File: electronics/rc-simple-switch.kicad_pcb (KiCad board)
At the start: 2 copper layers, 9 parts, among them K1 CONN_3, K2 CONN_3, P1 CONN_5, Q1 PMV30UN, U1 PIC10F200

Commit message: Tweak the PCB
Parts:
- added P2: CONN_1, Test_pad_1mm, F.Cu at (41.0, 41.0)
- added P3: CONN_1, Test_pad_1mm, F.Cu at (46.0, 38.0)
- added P4: CONN_1, Test_pad_1mm, F.Cu at (41.0, 39.5)
- added P5: CONN_1, Test_pad_1mm, F.Cu at (46.0, 39.5)
- P1: value CONN_5 -> CONN_1; footprint debug_connector -> Test_pad_1mm
- moved R2 5.69 mm to (45.0, 42.9), turned to 270 degrees
- moved C1 4.04 mm to (42.7, 42.9), turned to 270 degrees
- moved Q1 2.74 mm to (47.8, 42.4)
- moved U1 2.71 mm to (43.5, 39.5)
- moved K2 2.54 mm to (50.8, 40.6)
- moved P1 2.47 mm to (41.0, 38.0)
- moved R1 0.52 mm to (38.9, 38.9)
- moved D1 0.40 mm to (38.9, 42.4), turned to 0 degrees
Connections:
- P1 pad 1: VSS -> N-000005
- R1 pad 2: /ICSPDAT -> N-000005
- U1 pad 1: /ICSPDAT -> N-000005
- U1 pad 3: /ICSPCLK -> N-000004
- U1 pad 6: /VPP -> N-000003
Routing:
- net VSS: track 36.6 -> 18.4 mm, vias 3 -> 0
- net /ICSPCLK: track 6.70 -> 0.00 mm
- net /ICSPDAT: track 5.95 -> 0.00 mm
- net /OUT: track 10.6 -> 4.69 mm
- net VDD: track 13.1 -> 7.88 mm
- net VCC: track 23.7 -> 19.2 mm
- net N-000005: track 0.00 -> 4.35 mm
- net /VPP: track 2.59 -> 0.00 mm
- net N-000004: track 0.00 -> 1.46 mm
- net N-000003: track 0.00 -> 1.46 mm
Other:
- net class Power added: clearance 0.508, trace_width 0.254, via_dia 0.889, via_drill 0.635
- board text added: "1"

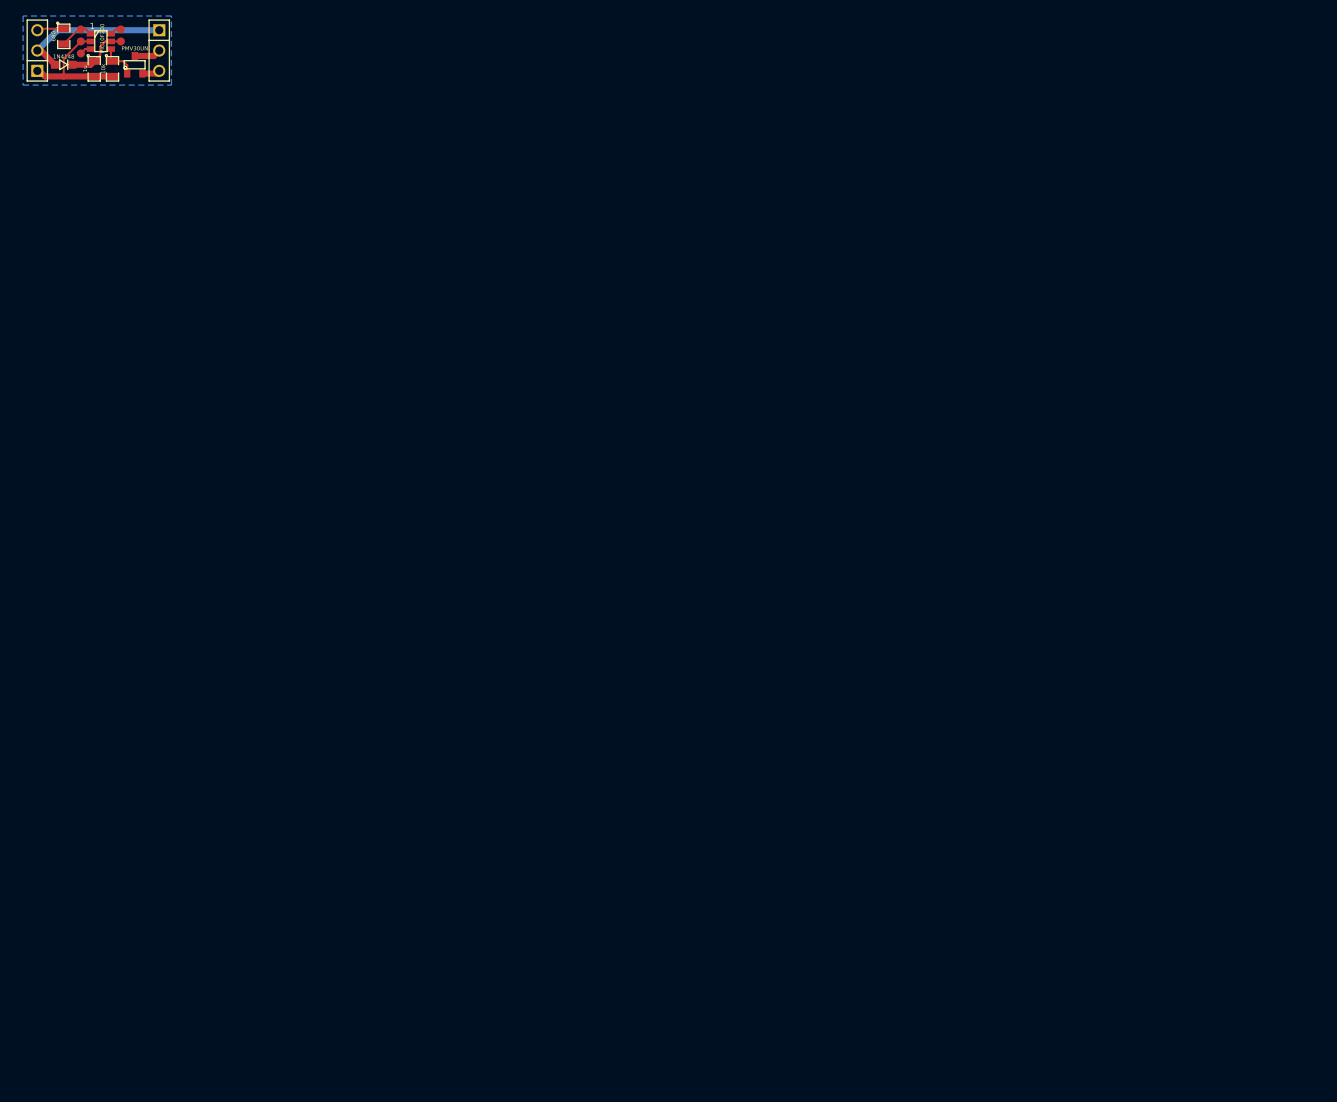
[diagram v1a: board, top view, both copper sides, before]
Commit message: Make the board smaller and re-orient output connector
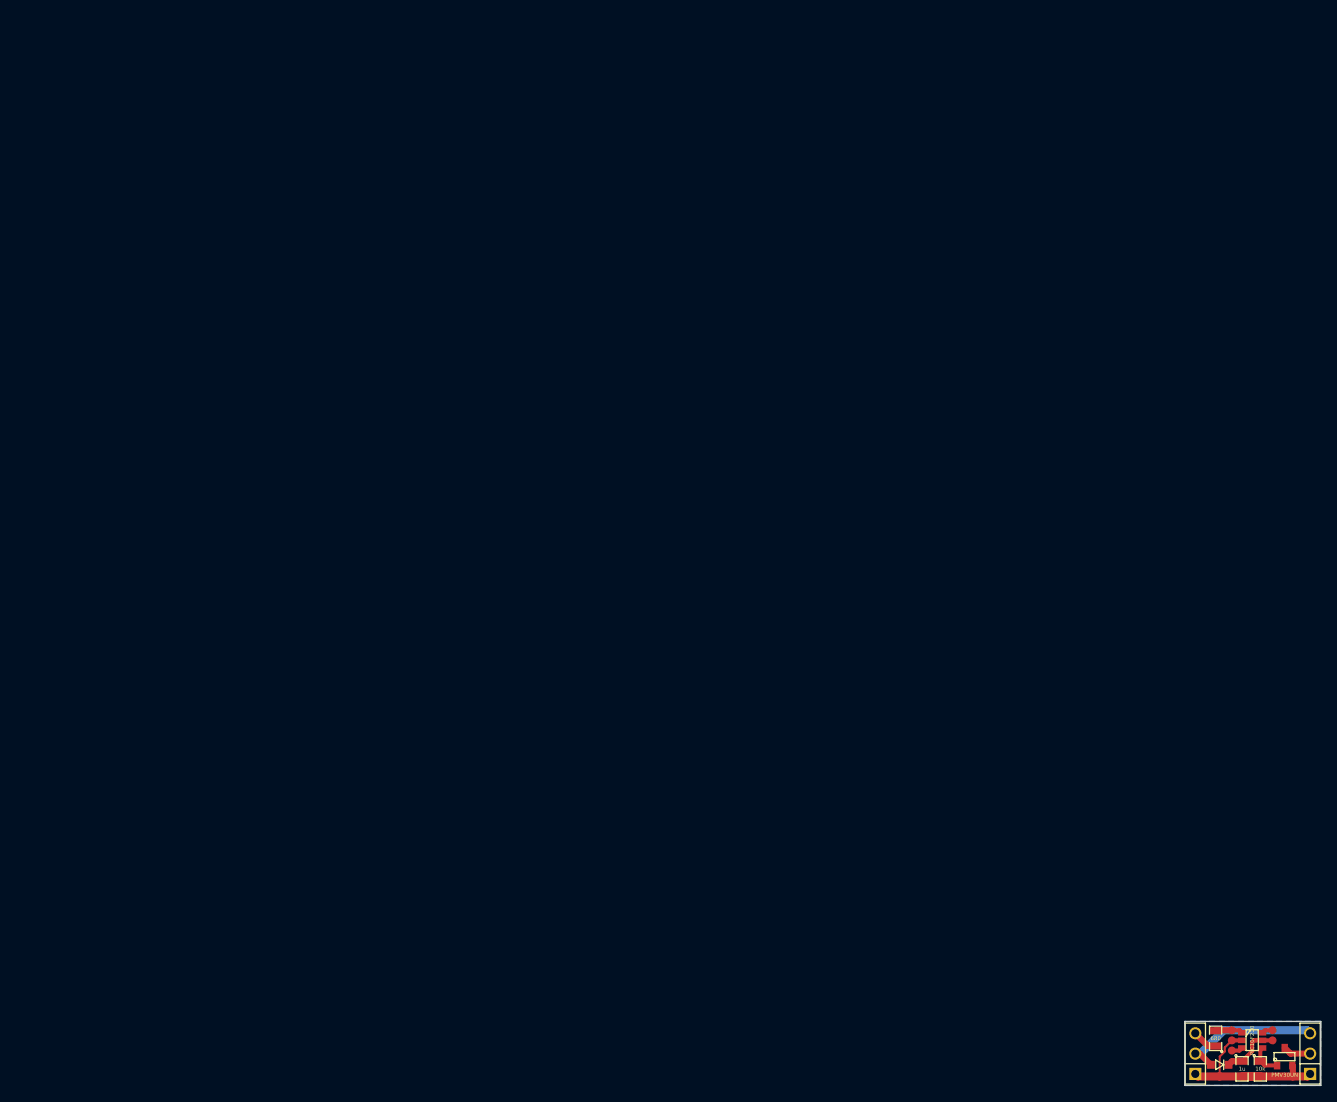
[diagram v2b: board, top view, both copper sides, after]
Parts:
- moved K1 191.5 mm to (180.3, 166.0)
- moved D1 191.1 mm to (183.4, 167.4)
- moved R1 190.8 mm to (182.8, 164.1), turned to 90 degrees
- moved K2 190.8 mm to (194.7, 166.0), turned to 90 degrees
- moved P3 190.7 mm to (190.0, 163.1)
- moved P1 190.7 mm to (184.9, 163.1)
- moved P5 190.6 mm to (190.0, 164.4)
- moved U1 190.5 mm to (187.4, 164.4)
- moved P4 190.5 mm to (184.9, 164.4)
- moved P2 190.4 mm to (184.9, 165.6)
- moved C1 190.3 mm to (186.1, 167.9)
- moved R2 190.3 mm to (188.4, 167.9)
- moved Q1 189.8 mm to (191.5, 166.4)
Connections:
- K2 pad 1: VCC -> VSS
- K2 pad 3: VSS -> VCC
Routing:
- net VSS: track 18.4 -> 24.7 mm
- net VCC: track 19.2 -> 18.2 mm
- net N-000007: track 4.35 -> 3.46 mm
- net /OUT: track 4.69 -> 4.07 mm
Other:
- board outline added: 17 x 8 mm
- net class Default: clearance 0.254 -> 0.1524
- rule trace_clearance: 0.254 -> 0.1524
- board text added: "+"
- board text added: "-"
- board text added: "LANE Boys RC"
- board text added: "RC on/off switch"
- board text added: "S"
- board text removed: "1"
